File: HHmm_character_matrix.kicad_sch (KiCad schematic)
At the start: 20 parts, among them U22 SN74LVC244A, U23 SM411006N/15, U24 SN74LVC244A, U25 SM411006N/15, U26 SM411006N/15, U27 SM411006N/15

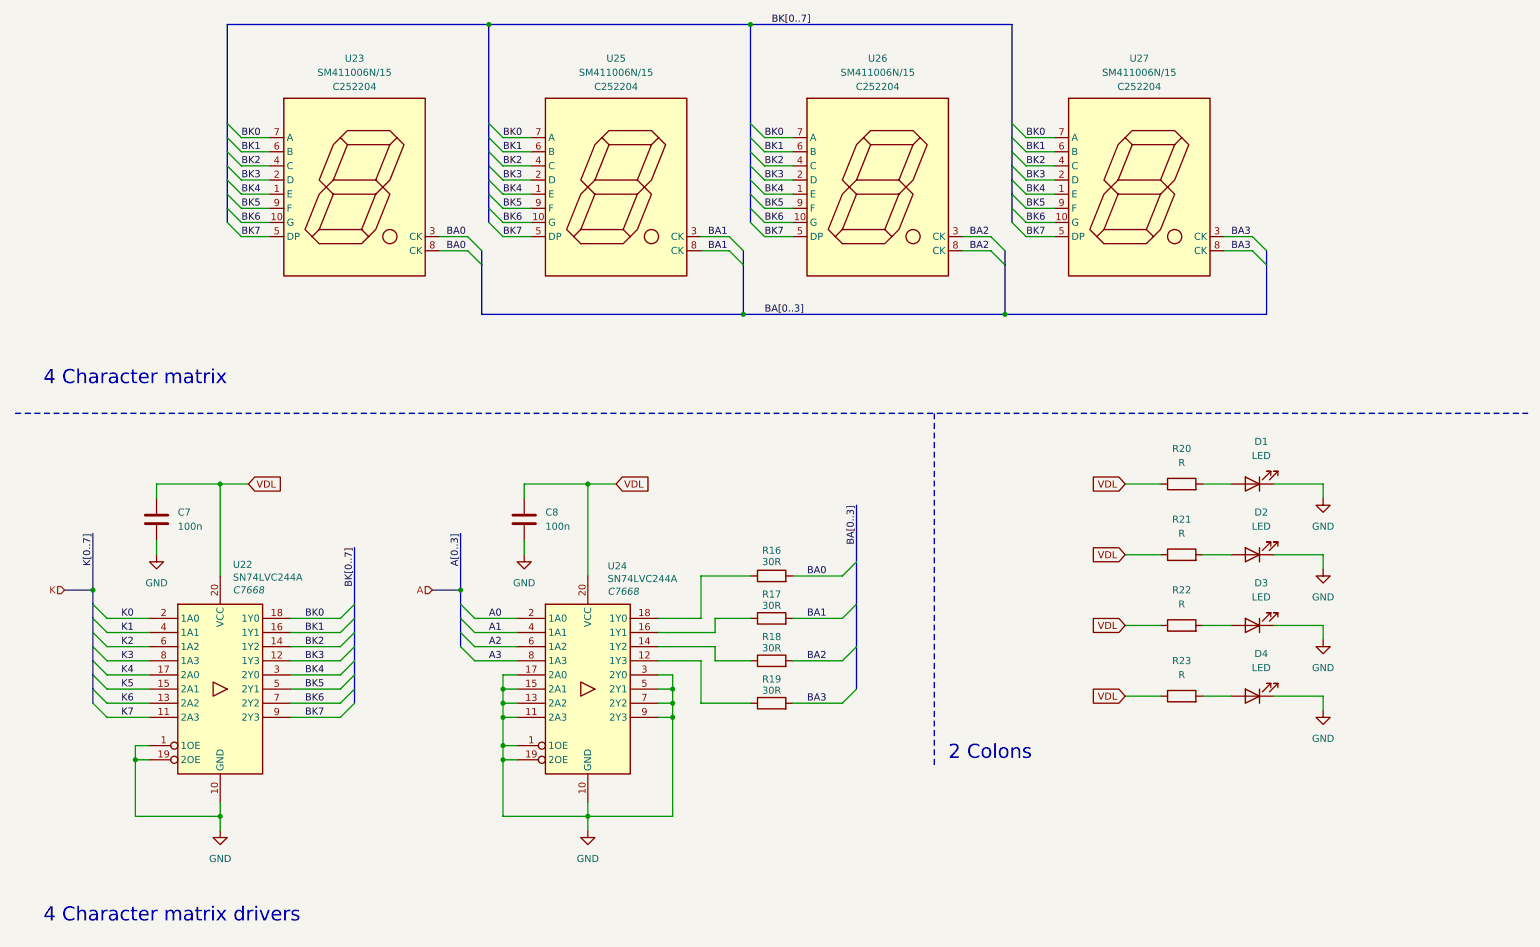
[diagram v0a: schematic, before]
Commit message: addition of bus
- cleaned up the structure of the schematic.
- addition of the colon
- root schematic improvements
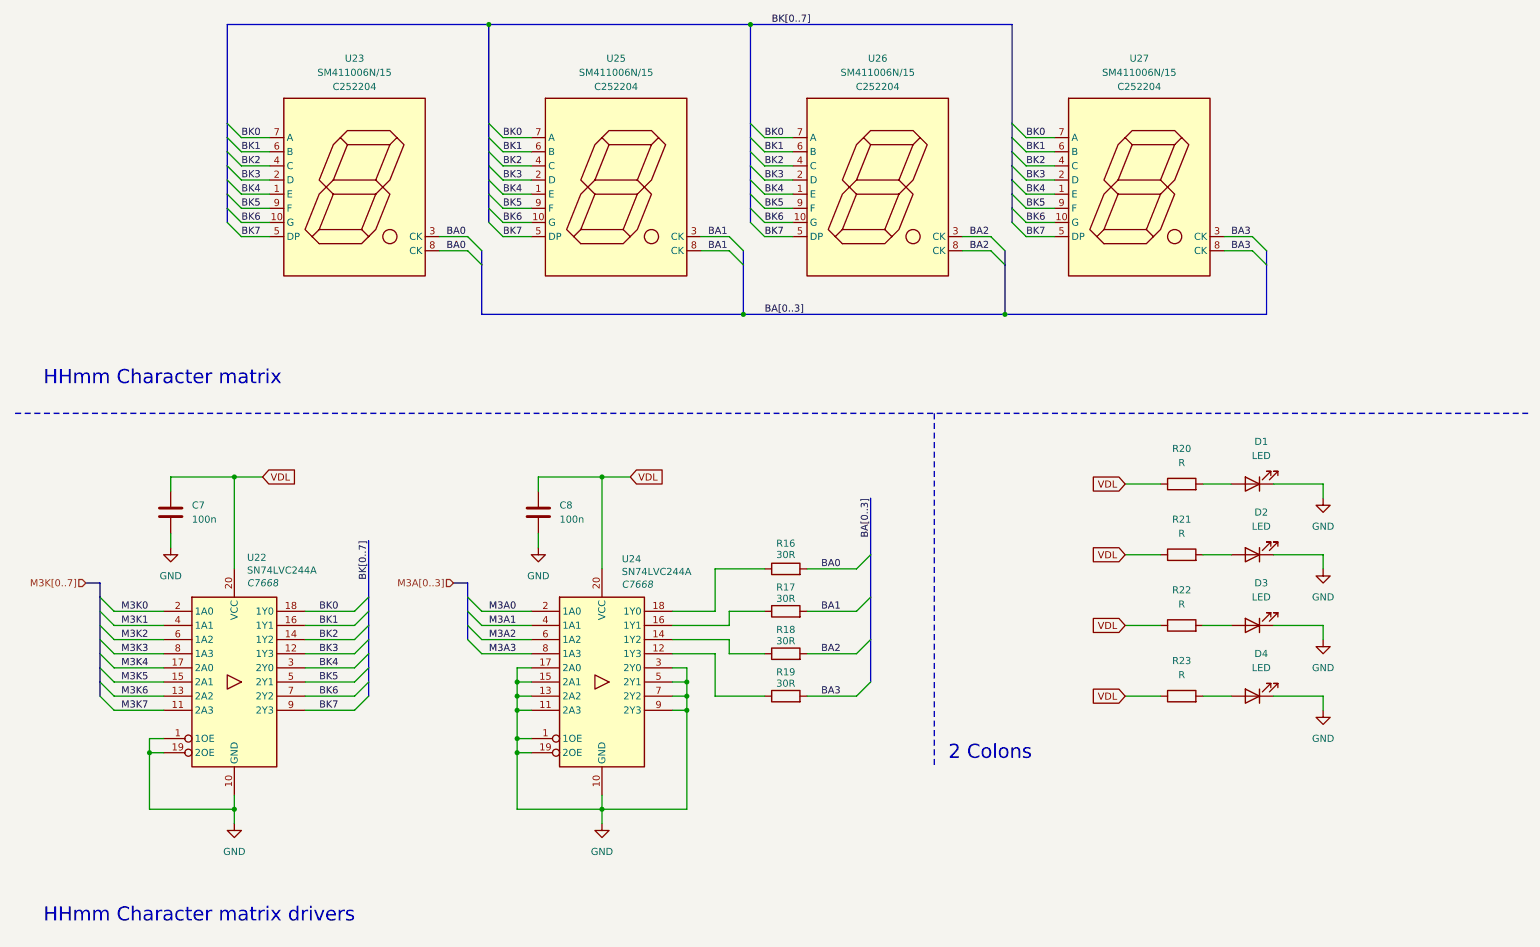
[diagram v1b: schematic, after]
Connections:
- net A0 renamed M3A0
- net A1 renamed M3A1
- net A2 renamed M3A2
- net A3 renamed M3A3
- net K0 renamed M3K0
- net K1 renamed M3K1
- net K2 renamed M3K2
- net K3 renamed M3K3
- net K4 renamed M3K4
- net K5 renamed M3K5
- net K6 renamed M3K6
- net K7 renamed M3K7
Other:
- note added: "HHmm Character matrix"
- note added: "HHmm Character matrix drivers"
- note removed: "4 Character matrix"
- note removed: "4 Character matrix drivers"
- title: (none) -> HHmm Character Matrix & Drivers 
- moved on the sheet: C7, C8, R16, R17, R18, R19, U22, U24

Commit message: current limiting resistor changes
- added colon led model, but might replace it in the future.
- reduction in current limiting resistance.
- removed the solder jumps in the individual circuit schematics.
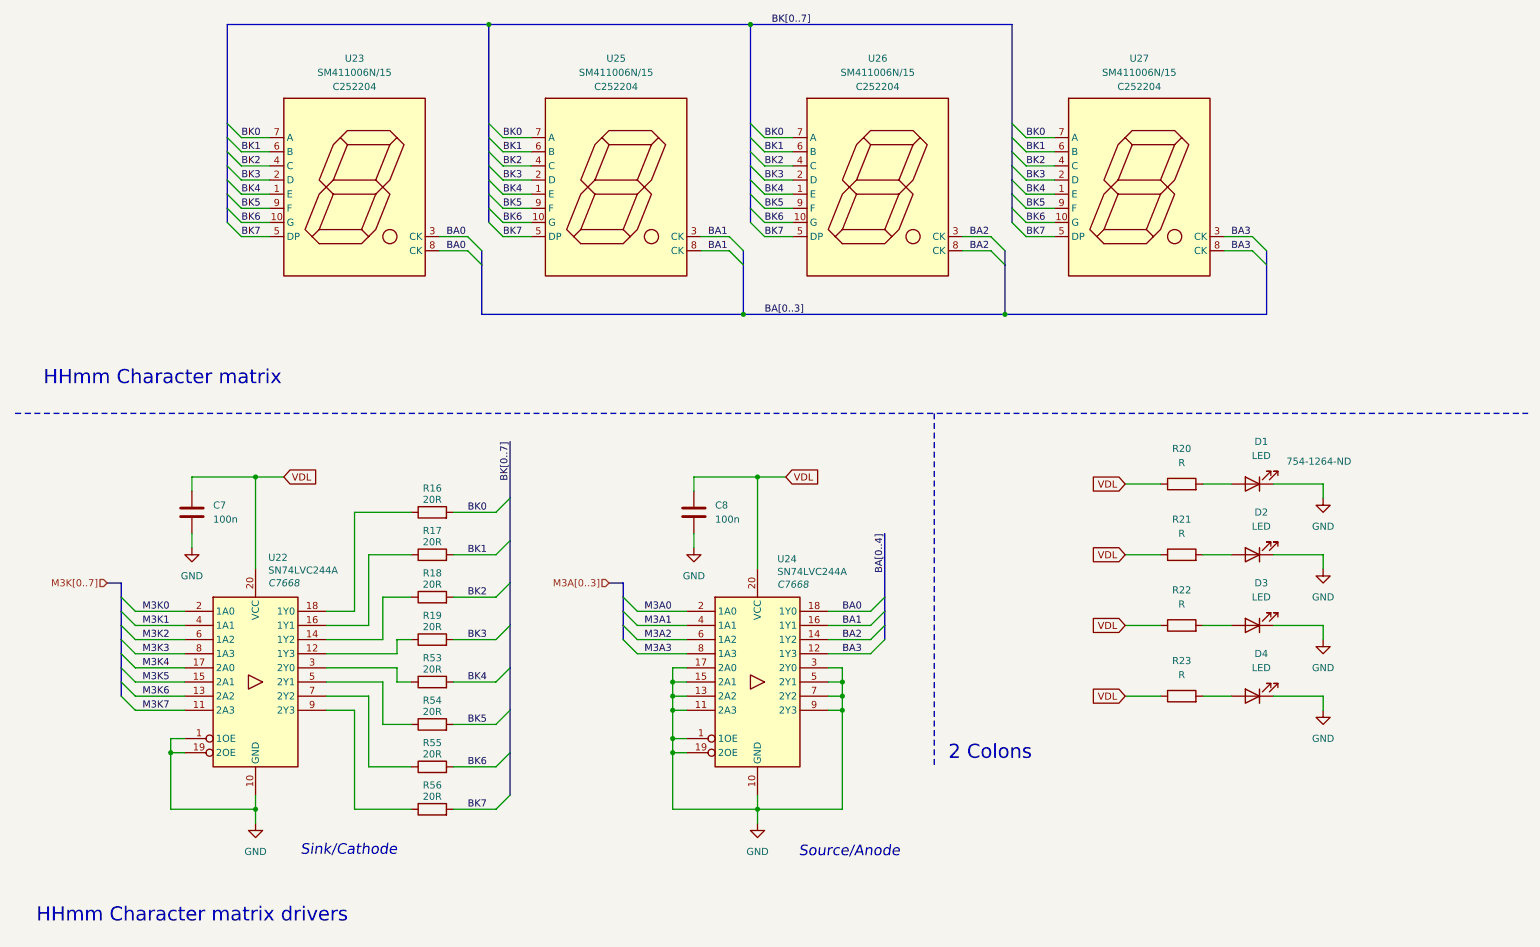
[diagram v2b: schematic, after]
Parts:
- added R53, R54, R55, R56: 20R, symbol Device:R
- D1: Digikey (none) -> 754-1264-ND
- R16, R17, R18, R19: value 30R -> 20R
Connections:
- net BA0: now also U24.18 (1Y0); no longer R16.2
- net BA1: now also U24.16 (1Y1); no longer R17.2
- net BA2: now also U24.14 (1Y2); no longer R18.2
- net BA3: now also U24.12 (1Y3); no longer R19.2
- net BK0: now also R16.2; no longer U22.18 (1Y0)
- net BK1: now also R17.2; no longer U22.16 (1Y1)
- net BK2: now also R18.2; no longer U22.14 (1Y2)
- net BK3: now also R19.2; no longer U22.12 (1Y3)
- net BK4: now also R53.2; no longer U22.3 (2Y0)
- net BK5: now also R54.2; no longer U22.5 (2Y1)
- net BK6: now also R55.2; no longer U22.7 (2Y2)
- net BK7: now also R56.2; no longer U22.9 (2Y3)
- net at R19.1: now also U22.12 (1Y3); no longer U24.12 (1Y3)
- net at R18.1: now also U22.14 (1Y2); no longer U24.14 (1Y2)
- net at R17.1: now also U22.16 (1Y1); no longer U24.16 (1Y1)
- net at R16.1: now also U22.18 (1Y0); no longer U24.18 (1Y0)
- new net: R54.1, U22.5 (2Y1)
- new net: R55.1, U22.7 (2Y2)
- new net: R53.1, U22.3 (2Y0)
- new net: R56.1, U22.9 (2Y3)
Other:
- note added: "Sink/Cathode"
- note added: "Source/Anode"

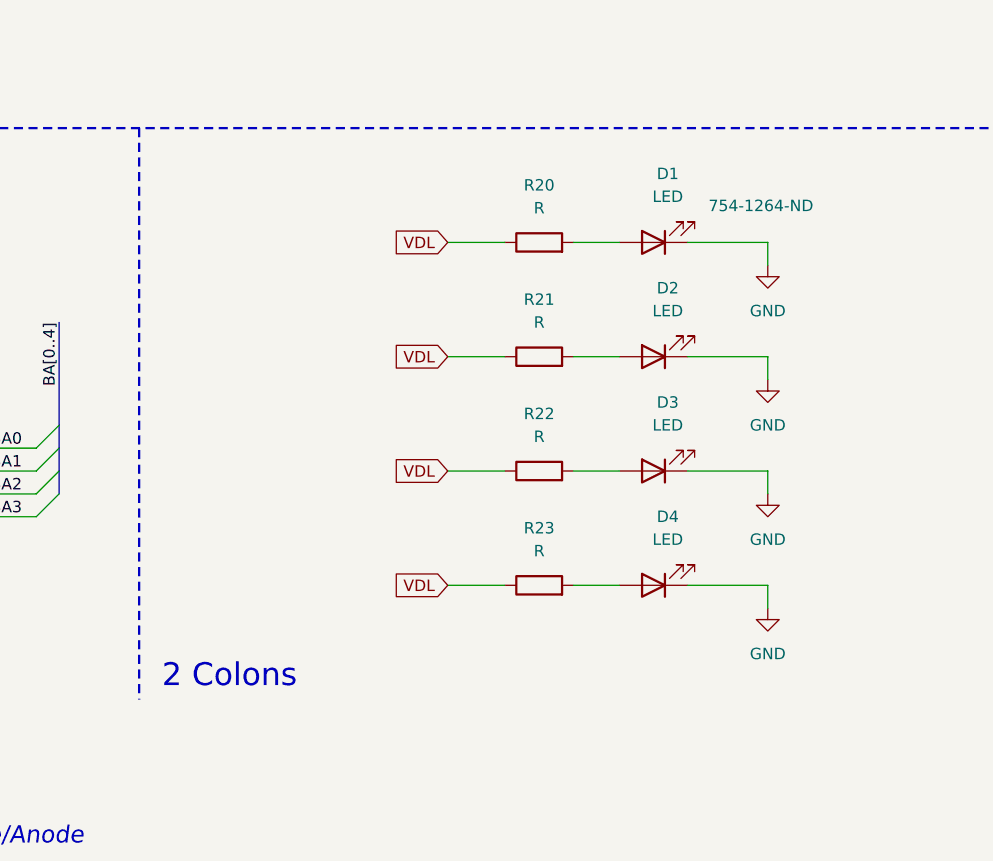
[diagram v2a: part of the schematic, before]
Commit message: voltage regulation changes
- ambient light sensor addition
- colon control
- brightness control through regulators
- added test points
- MCU pinout changes
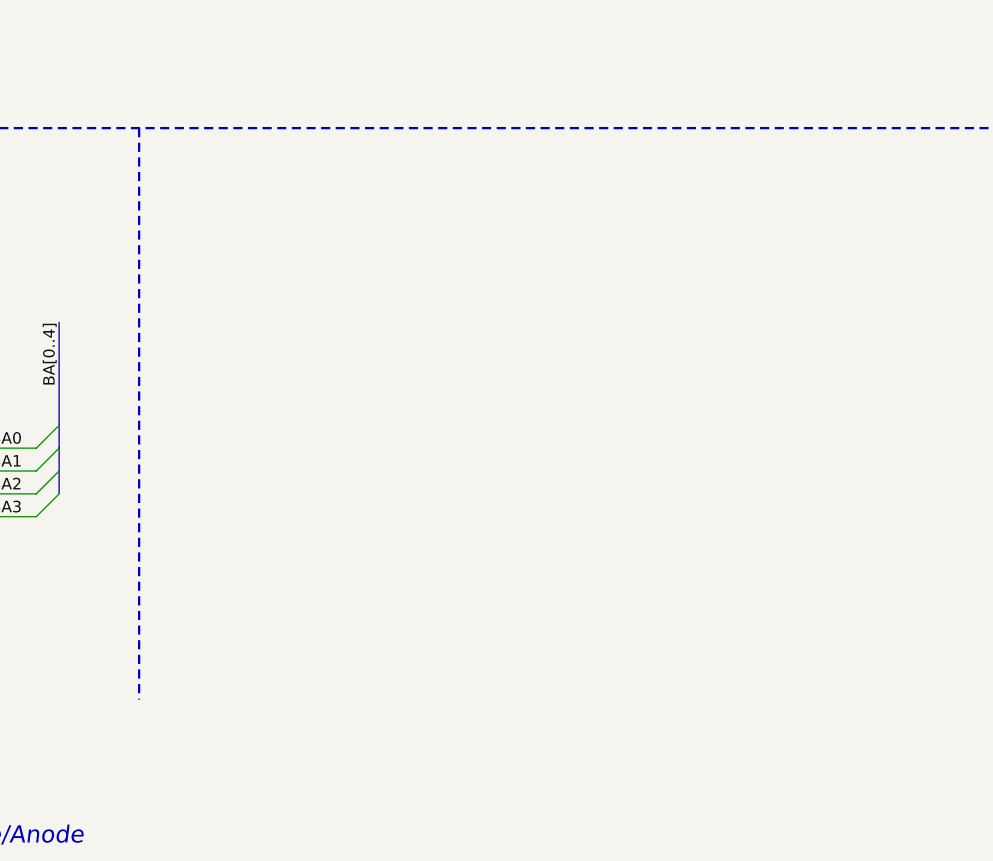
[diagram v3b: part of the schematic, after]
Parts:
- removed D1, D2, D3, D4: LED, symbol Device:LED
- removed R20, R21, R22, R23: R, symbol Device:R
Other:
- note removed: "2 Colons"

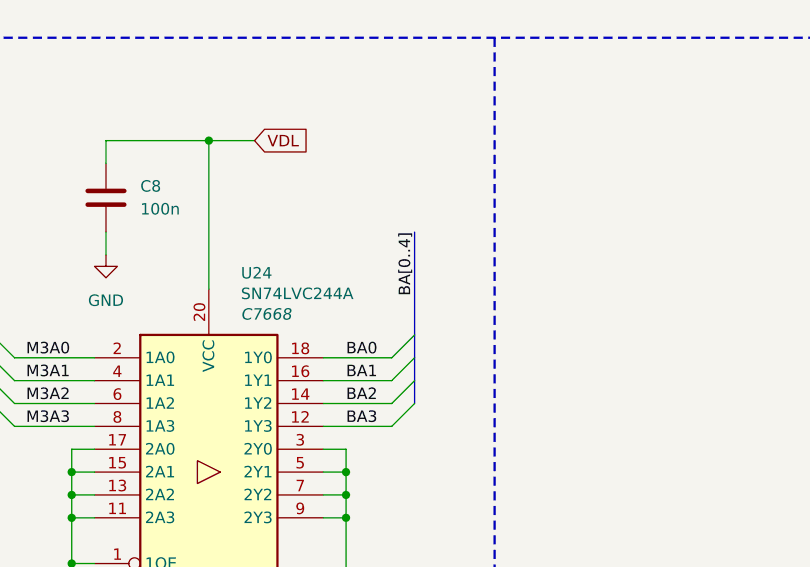
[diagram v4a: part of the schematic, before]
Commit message: Buzzer driver added - replacement of photoresistor to a variable resistor - added button - general formatting
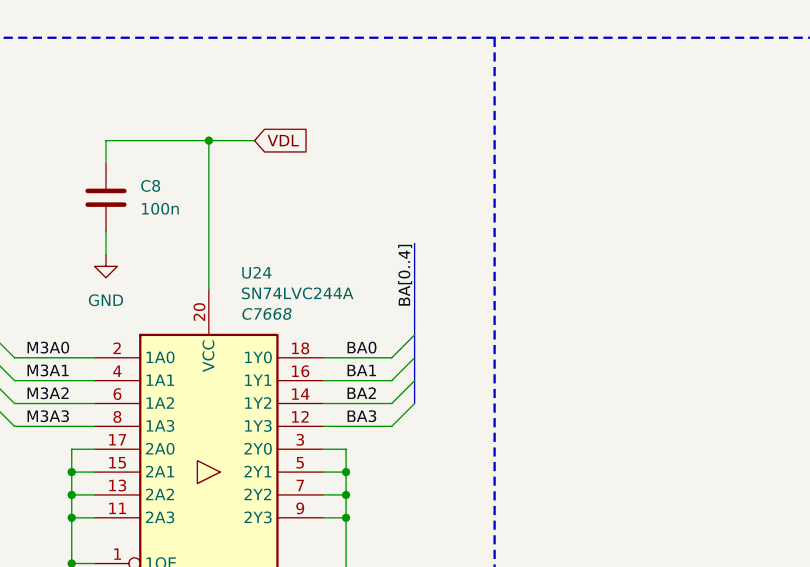
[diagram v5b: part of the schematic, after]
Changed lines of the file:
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@@
 	(bus
 		(pts
-			(xy 168.91 123.19) (xy 168.91 134.62)
+			(xy 168.91 124.46) (xy 168.91 134.62)
 		)
 		(stroke
@@
 	)
 	(label "BA[0..4]"
-		(at 168.91 123.19 270)
-		(effects
-			(font
+		(at 168.91 124.46 270)
+		(effects
+			(font

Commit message: ESD, LEDs, footprints
- assignment of footprints
- ESD protection
- User buttons
- addition of test points
- BOM consolidation of  resistors
- general reordering of the schematic
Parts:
- C7, C8: footprint (none) -> Capacitor_SMD:C_0603_1608Metric
- R16, R17, R18, R19, R53, R54, R55, R56: footprint (none) -> Resistor_SMD:R_0603_1608Metric
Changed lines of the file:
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@@
 	(title_block
 		(title "HHmm Character Matrix & Drivers ")
-		(date "2025-10-31")
+		(date "2025-11-04")
 		(rev "v0.0")
 		(company "Rajath Katker")
@@
 			)
 		)
-		(property "Footprint" ""
+		(property "Footprint" "Capacitor_SMD:C_0603_1608Metric"
 			(at 45.4152 123.19 0)
 			(effects
@@
 			)
 		)
-		(property "Footprint" ""
+		(property "Footprint" "Resistor_SMD:R_0603_1608Metric"
 			(at 87.63 159.258 90)
 			(effects
@@
 			)
 		)
-		(property "Footprint" ""
+		(property "Footprint" "Resistor_SMD:R_0603_1608Metric"
 			(at 87.63 166.878 90)
 			(effects
@@
 			)
 		)
-		(property "Footprint" ""
+		(property "Footprint" "Resistor_SMD:R_0603_1608Metric"
 			(at 87.63 144.018 90)
 			(effects
@@
 			)
 		)
-		(property "Footprint" ""
+		(property "Footprint" "Resistor_SMD:R_0603_1608Metric"
 			(at 87.63 128.778 90)
 			(effects
@@
 			)
 		)
-		(property "Footprint" ""
+		(property "Footprint" "Resistor_SMD:R_0603_1608Metric"
 			(at 87.63 174.498 90)
 			(effects
@@
 			)
 		)
-		(property "Footprint" ""
+		(property "Footprint" "Resistor_SMD:R_0603_1608Metric"
 			(at 87.63 151.638 90)
 			(effects
@@
 			)
 		)
-		(property "Footprint" ""
+		(property "Footprint" "Capacitor_SMD:C_0603_1608Metric"
 			(at 135.5852 123.19 0)
 			(effects
@@
 			)
 		)
-		(property "Footprint" ""
+		(property "Footprint" "Resistor_SMD:R_0603_1608Metric"
 			(at 87.63 121.158 90)
 			(effects
@@
 			)
 		)
-		(property "Footprint" ""
+		(property "Footprint" "Resistor_SMD:R_0603_1608Metric"
 			(at 87.63 136.398 90)
 			(effects
